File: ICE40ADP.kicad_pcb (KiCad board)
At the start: 2 copper layers, 5 parts, among them J1 Conn_02x20_Odd_Even, J2 Conn_02x20_Odd_Even, J3 Conn_02x20_Odd_Even, J4 Conn_02x20_Odd_Even, J5 Samtec_ASP-134486-01

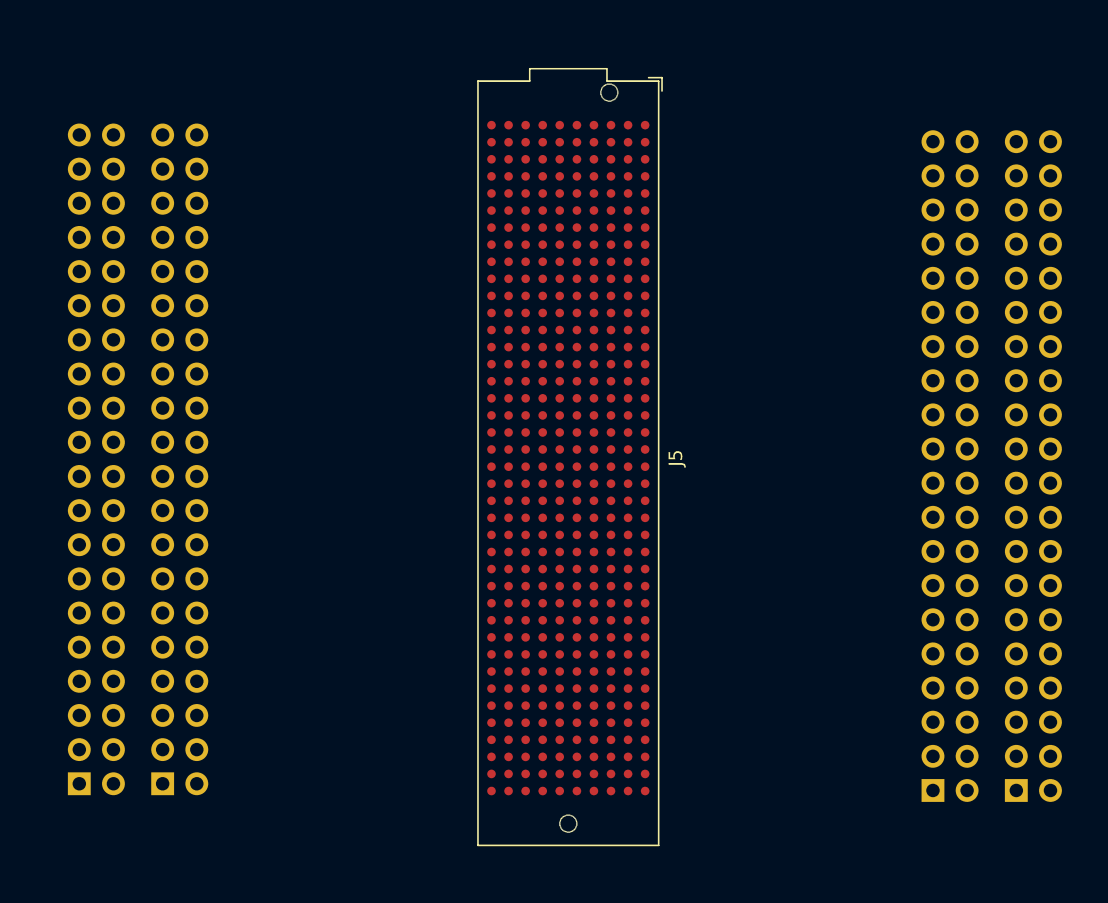
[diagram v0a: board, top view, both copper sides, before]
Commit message: LP lines added. Changed PCB connectors placement
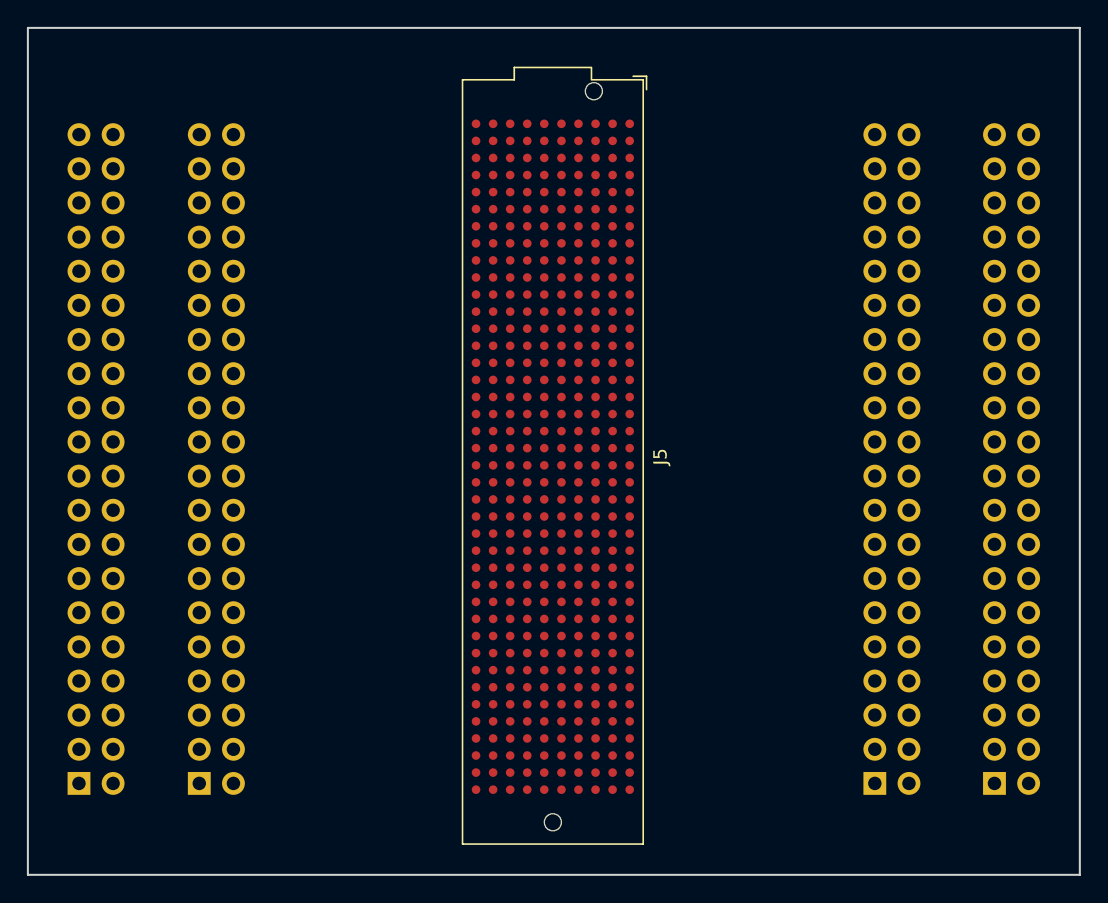
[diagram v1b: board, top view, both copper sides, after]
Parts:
- moved J3 4.36 mm to (170.3, 127.2)
- moved J2 2.73 mm to (120.0, 127.2)
- moved J4 1.71 mm to (179.2, 127.2)
- moved J5 1.15 mm to (146.3, 102.9)
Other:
- board outline added: 78.3 x 63 mm
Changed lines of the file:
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@@
   (general
     (thickness 1.6)
-    (drawings 0)
+    (drawings 4)
     (tracks 0)
     (zones 0)
@@
   )
   (module Connector_PinHeader_2.54mm:PinHeader_2x20_P2.54mm_Vertical (layer B.Cu)
-    (at 111.125001 127.225001)
+    (at 111.1 127.2)
     (descr "Through hole straight pin header, 2x20, 2.54mm pitch, double rows")
     (tags "Through hole pin header THT 2x20 2.54mm double row")
@@
       (effects (font (size 1 1) (thickness 0.15)) (justify mirror))
     )
-    (fp_text value Conn_02x20_Odd_Even (at 1.27 -50.59) (layer B.Fab)
+    (fp_text value Conn_02x20_Odd_Even (at 5.45 -25.35 90) (layer B.Fab)
       (effects (font (size 1 1) (thickness 0.15)) (justify mirror))
     )
@@
   )
   (module Connector_PinHeader_2.54mm:PinHeader_2x20_P2.54mm_Vertical (layer B.Cu)
-    (at 117.325001 127.225001)
+    (at 120.05 127.2)
     (descr "Through hole straight pin header, 2x20, 2.54mm pitch, double rows")
     (tags "Through hole pin header THT 2x20 2.54mm double row")
@@
       (effects (font (size 1 1) (thickness 0.15)) (justify mirror))
     )
-    (fp_text value Conn_02x20_Odd_Even (at 1.27 -50.59) (layer B.Fab)
+    (fp_text value Conn_02x20_Odd_Even (at 5.725 -25.425 90) (layer B.Fab)
       (effects (font (size 1 1) (thickness 0.15)) (justify mirror))
     )
@@
   )
   (module Connector_PinHeader_2.54mm:PinHeader_2x20_P2.54mm_Vertical (layer B.Cu)
-    (at 174.625001 127.725001)
+    (at 170.3 127.2)
     (descr "Through hole straight pin header, 2x20, 2.54mm pitch, double rows")
     (tags "Through hole pin header THT 2x20 2.54mm double row")
@@
       (effects (font (size 1 1) (thickness 0.15)) (justify mirror))
     )
-    (fp_text value Conn_02x20_Odd_Even (at 1.27 -50.59) (layer B.Fab)
+    (fp_text value Conn_02x20_Odd_Even (at -3.275 -25.85 90) (layer B.Fab)
       (effects (font (size 1 1) (thickness 0.15)) (justify mirror))
     )
@@
   )
   (module Connector_PinHeader_2.54mm:PinHeader_2x20_P2.54mm_Vertical (layer B.Cu)
-    (at 180.825001 127.725001)
+    (at 179.2 127.2)
     (descr "Through hole straight pin header, 2x20, 2.54mm pitch, double rows")
     (tags "Through hole pin header THT 2x20 2.54mm double row")
@@
       (effects (font (size 1 1) (thickness 0.15)) (justify mirror))
     )
-    (fp_text value Conn_02x20_Odd_Even (at 1.27 -50.59) (layer B.Fab)
+    (fp_text value Conn_02x20_Odd_Even (at -3 -25.925 90) (layer B.Fab)
       (effects (font (size 1 1) (thickness 0.15)) (justify mirror))
     )
@@
   )
   (module Connector_Samtec:Samtec_FMC_ASP-134486-01_10x40_P1.27mm_Vertical (layer F.Cu)
-    (at 147.5 103 270)
+    (at 146.35 102.9 270)
     (descr http://suddendocs.samtec.com/prints/asp-134486-01-mkt.pdf)
     (tags "FMC HPC")
@@
     )
   )
+  (gr_line (start 107.3 71) (end 185.55 71) (layer Edge.Cuts) (width 0.15))
+  (gr_line (start 107.3 134) (end 185.55 134) (layer Edge.Cuts) (width 0.15))
+  (gr_line (start 107.3 71) (end 107.3 134) (layer Edge.Cuts) (width 0.15))
+  (gr_line (start 185.55 71) (end 185.55 134) (layer Edge.Cuts) (width 0.15))
 )

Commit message: First version of routing
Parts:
- added C1: 4.7uF, Capacitor_SMD:C_0402_1005Metric, B.Cu at (138.6, 123.0)
- added D1: PGB1010603NRHF, Diode_SMD:D_0603_1608Metric, B.Cu at (138.3, 130.4)
- added J6: Micro_SD_Card_Det, Connector_Card:microSD_HC_Hirose_DM3D-SF, B.Cu at (146.4, 127.4)
- added R1: 100K, Resistor_SMD:R_0402_1005Metric, B.Cu at (135.1, 131.2)
- added TP1: TestPoint, TestPoint:TestPoint_Pad_D1.5mm, B.Cu at (146.3, 74.0)
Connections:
- J1 pad 10: (no net) -> CHIPLINK_TX_DAT5
- J1 pad 11: (no net) -> CHIPLINK_TX_DAT4
- J1 pad 12: (no net) -> CHIPLINK_TX_DAT6
- J1 pad 13: (no net) -> CHIPLINK_TX_DAT9
- J1 pad 14: (no net) -> CHIPLINK_TX_DAT10
- J1 pad 15: (no net) -> Earth
- J1 pad 16: (no net) -> Earth
- J1 pad 17: (no net) -> CHIPLINK_TX_DAT7
- J1 pad 18: (no net) -> CHIPLINK_TX_DAT11
- J1 pad 19: (no net) -> CHIPLINK_TX_DAT17
- J1 pad 2: (no net) -> +1V8
- J1 pad 20: (no net) -> CHIPLINK_TX_DAT20
- J1 pad 21: (no net) -> CHIPLINK_TX_DAT8
- J1 pad 22: (no net) -> CHIPLINK_TX_DAT12
- J1 pad 23: (no net) -> Earth
- J1 pad 24: (no net) -> Earth
- J1 pad 25: (no net) -> CHIPLINK_TX_CLK
- J1 pad 26: (no net) -> CHIPLINK_TX_DAT14
- J1 pad 27: (no net) -> CHIPLINK_TX_DAT13
- J1 pad 28: (no net) -> CHIPLINK_TX_DAT16
- J1 pad 29: (no net) -> CHIPLINK_TX_DAT15
- J1 pad 30: (no net) -> CHIPLINK_TX_DAT22
- J1 pad 31: (no net) -> Earth
- J1 pad 32: (no net) -> Earth
- J1 pad 33: (no net) -> CHIPLINK_TX_DAT18
- J1 pad 34: (no net) -> CHIPLINK_TX_DAT21
- J1 pad 35: (no net) -> CHIPLINK_TX_DAT19
- J1 pad 36: (no net) -> CHIPLINK_TX_DAT25
- J1 pad 37: (no net) -> CHIPLINK_TX_DAT23
- J1 pad 38: (no net) -> CHIPLINK_TX_DAT24
- J1 pad 39: (no net) -> Earth
- J1 pad 4: (no net) -> CHIPLINK_TX_DAT0
- J1 pad 40: (no net) -> Earth
- J1 pad 5: (no net) -> CHIPLINK_TX_DAT2
- J1 pad 6: (no net) -> CHIPLINK_TX_DAT1
- J1 pad 7: (no net) -> Earth
- J1 pad 8: (no net) -> Earth
- J1 pad 9: (no net) -> CHIPLINK_TX_DAT3
- J2 pad 1: (no net) -> /Sheet5CA0FCBB/SDIO_DAT2
- J2 pad 15: (no net) -> Earth
- J2 pad 16: (no net) -> Earth
- J2 pad 2: (no net) -> /Sheet5CA0FCBB/+3V3
- J2 pad 23: (no net) -> Earth
- J2 pad 24: (no net) -> Earth
- J2 pad 3: (no net) -> /Sheet5CA0FCBB/SDIO_DAT3
- J2 pad 31: (no net) -> Earth
- J2 pad 32: (no net) -> Earth
- J2 pad 39: (no net) -> Earth
- J2 pad 4: (no net) -> /Sheet5CA0FCBB/SDIO_DAT0
- J2 pad 40: (no net) -> Earth
- J2 pad 5: (no net) -> /Sheet5CA0FCBB/SDIO_CMD
- J2 pad 6: (no net) -> /Sheet5CA0FCBB/SDIO_DAT1
- J2 pad 7: (no net) -> Earth
- J2 pad 8: (no net) -> Earth
- J2 pad 9: (no net) -> /Sheet5CA0FCBB/SDIO_CLK
- J3 pad 1: (no net) -> CHIPLINK_RX_DAT26
- J3 pad 11: (no net) -> CHIPLINK_RX_DAT18
- J3 pad 12: (no net) -> CHIPLINK_RX_DAT22
- J3 pad 13: (no net) -> CHIPLINK_RX_DAT19
- J3 pad 14: (no net) -> CHIPLINK_RX_DAT16
- J3 pad 15: (no net) -> Earth
- J3 pad 16: (no net) -> Earth
- J3 pad 17: (no net) -> CHIPLINK_RX_DAT17
- J3 pad 18: (no net) -> CHIPLINK_RX_DAT15
- J3 pad 19: (no net) -> CHIPLINK_RX_DAT9
- J3 pad 2: (no net) -> +1V8
- J3 pad 20: (no net) -> CHIPLINK_RX_DAT14
- J3 pad 21: (no net) -> CHIPLINK_RX_DAT13
- J3 pad 22: (no net) -> CHIPLINK_RX_CLK
- J3 pad 23: (no net) -> Earth
- J3 pad 24: (no net) -> Earth
- J3 pad 25: (no net) -> CHIPLINK_RX_DAT11
- J3 pad 26: (no net) -> CHIPLINK_RX_DAT12
- J3 pad 27: (no net) -> CHIPLINK_RX_DAT10
- J3 pad 28: (no net) -> CHIPLINK_RX_DAT8
- J3 pad 29: (no net) -> CHIPLINK_RX_DAT7
- J3 pad 3: (no net) -> CHIPLINK_RX_DAT20
- J3 pad 30: (no net) -> CHIPLINK_RX_DAT4
- J3 pad 31: (no net) -> Earth
- J3 pad 32: (no net) -> Earth
- J3 pad 33: (no net) -> CHIPLINK_RX_DAT3
- J3 pad 34: (no net) -> CHIPLINK_RX_DAT6
- J3 pad 35: (no net) -> CHIPLINK_RX_DAT1
- J3 pad 36: (no net) -> CHIPLINK_RX_DAT5
- J3 pad 37: (no net) -> CHIPLINK_RX_DAT0
- J3 pad 38: (no net) -> CHIPLINK_RX_DAT2
- J3 pad 39: (no net) -> Earth
- J3 pad 4: (no net) -> CHIPLINK_RX_DAT25
- J3 pad 40: (no net) -> Earth
- J3 pad 5: (no net) -> CHIPLINK_RX_DAT23
- J3 pad 6: (no net) -> CHIPLINK_RX_DAT21
- J3 pad 7: (no net) -> Earth
- J3 pad 8: (no net) -> Earth
- J3 pad 9: (no net) -> CHIPLINK_RX_DAT24
- J4 pad 15: (no net) -> Earth
- J4 pad 16: (no net) -> Earth
- J4 pad 18: (no net) -> CHIPLINK_RX_DAT27
- J4 pad 2: (no net) -> +1V8
- J4 pad 20: (no net) -> CHIPLINK_TX_RST
- J4 pad 21: (no net) -> CHIPLINK_RX_SEND
- J4 pad 23: (no net) -> Earth
- J4 pad 24: (no net) -> Earth
- J4 pad 25: (no net) -> CHIPLINK_RX_DAT31
- J4 pad 26: (no net) -> CHIPLINK_RX_RST
- J4 pad 27: (no net) -> CHIPLINK_RX_DAT29
- J4 pad 28: (no net) -> CHIPLINK_TX_SEND
- J4 pad 29: (no net) -> CHIPLINK_RX_DAT28
- J4 pad 30: (no net) -> CHIPLINK_RX_DAT30
- J4 pad 31: (no net) -> Earth
- J4 pad 32: (no net) -> Earth
- J4 pad 33: (no net) -> CHIPLINK_TX_DAT31
- J4 pad 34: (no net) -> CHIPLINK_TX_DAT30
- J4 pad 35: (no net) -> CHIPLINK_TX_DAT28
- J4 pad 36: (no net) -> CHIPLINK_TX_DAT29
- J4 pad 37: (no net) -> CHIPLINK_TX_DAT27
- J4 pad 38: (no net) -> CHIPLINK_TX_DAT26
- J4 pad 39: (no net) -> Earth
- J4 pad 4: (no net) -> RESET_N
- J4 pad 40: (no net) -> Earth
- J4 pad 6: (no net) -> /Sheet5CA0FCBB/SDIO_CD
- J4 pad 7: (no net) -> Earth
- J4 pad 8: (no net) -> Earth
- J5 pad A1: (no net) -> Earth
- J5 pad A12: (no net) -> Earth
- J5 pad A13: (no net) -> Earth
- J5 pad A16: (no net) -> Earth
- J5 pad A17: (no net) -> Earth
- J5 pad A20: (no net) -> Earth
- J5 pad A21: (no net) -> Earth
- J5 pad A24: (no net) -> Earth
- J5 pad A25: (no net) -> Earth
- J5 pad A28: (no net) -> Earth
- J5 pad A29: (no net) -> Earth
- J5 pad A32: (no net) -> Earth
- J5 pad A33: (no net) -> Earth
- J5 pad A36: (no net) -> Earth
- J5 pad A37: (no net) -> Earth
- J5 pad A4: (no net) -> Earth
- J5 pad A40: (no net) -> Earth
- J5 pad A5: (no net) -> Earth
- J5 pad A8: (no net) -> Earth
- J5 pad A9: (no net) -> Earth
- J5 pad B10: (no net) -> Earth
- J5 pad B11: (no net) -> Earth
- J5 pad B14: (no net) -> Earth
- J5 pad B15: (no net) -> Earth
- J5 pad B18: (no net) -> Earth
- J5 pad B19: (no net) -> Earth
- J5 pad B2: (no net) -> Earth
- J5 pad B22: (no net) -> Earth
- J5 pad B23: (no net) -> Earth
- J5 pad B26: (no net) -> Earth
- J5 pad B27: (no net) -> Earth
- J5 pad B3: (no net) -> Earth
- J5 pad B30: (no net) -> Earth
- J5 pad B31: (no net) -> Earth
- J5 pad B34: (no net) -> Earth
- J5 pad B35: (no net) -> Earth
- J5 pad B38: (no net) -> Earth
- J5 pad B39: (no net) -> Earth
- J5 pad B6: (no net) -> Earth
- J5 pad B7: (no net) -> Earth
- J5 pad C1: (no net) -> Earth
- J5 pad C10: (no net) -> CHIPLINK_TX_DAT12
- J5 pad C11: (no net) -> CHIPLINK_TX_DAT13
- J5 pad C12: (no net) -> Earth
- J5 pad C13: (no net) -> Earth
- J5 pad C14: (no net) -> CHIPLINK_TX_DAT20
- J5 pad C15: (no net) -> CHIPLINK_TX_DAT21
- J5 pad C16: (no net) -> Earth
- J5 pad C17: (no net) -> Earth
- J5 pad C18: (no net) -> CHIPLINK_TX_DAT28
- J5 pad C19: (no net) -> CHIPLINK_TX_DAT29
- J5 pad C20: (no net) -> Earth
- J5 pad C21: (no net) -> Earth
- J5 pad C22: (no net) -> CHIPLINK_RX_DAT2
- J5 pad C23: (no net) -> CHIPLINK_RX_DAT3
- J5 pad C24: (no net) -> Earth
- J5 pad C25: (no net) -> Earth
- J5 pad C26: (no net) -> CHIPLINK_RX_DAT20
- J5 pad C27: (no net) -> CHIPLINK_RX_DAT21
- J5 pad C28: (no net) -> Earth
- J5 pad C29: (no net) -> Earth
- J5 pad C32: (no net) -> Earth
- J5 pad C33: (no net) -> Earth
- J5 pad C35: (no net) -> /Sheet5CA0FCF5/12P0V_FMC
- J5 pad C36: (no net) -> Earth
- J5 pad C37: (no net) -> /Sheet5CA0FCF5/12P0V_FMC
- J5 pad C38: (no net) -> Earth
- J5 pad C4: (no net) -> Earth
- J5 pad C40: (no net) -> Earth
- J5 pad C5: (no net) -> Earth
- J5 pad C8: (no net) -> Earth
- J5 pad C9: (no net) -> Earth
- J5 pad D10: (no net) -> Earth
- J5 pad D11: (no net) -> CHIPLINK_TX_DAT10
- J5 pad D12: (no net) -> CHIPLINK_TX_DAT11
- J5 pad D13: (no net) -> Earth
- J5 pad D14: (no net) -> CHIPLINK_TX_DAT18
- J5 pad D15: (no net) -> CHIPLINK_TX_DAT19
- J5 pad D16: (no net) -> Earth
- J5 pad D17: (no net) -> CHIPLINK_TX_DAT26
- J5 pad D18: (no net) -> CHIPLINK_TX_DAT27
- J5 pad D19: (no net) -> Earth
- J5 pad D2: (no net) -> Earth
- J5 pad D20: (no net) -> CHIPLINK_RX_DAT0
- J5 pad D21: (no net) -> CHIPLINK_RX_DAT1
- J5 pad D22: (no net) -> Earth
- J5 pad D23: (no net) -> CHIPLINK_RX_DAT12
- J5 pad D24: (no net) -> CHIPLINK_RX_DAT13
- J5 pad D25: (no net) -> Earth
- J5 pad D26: (no net) -> CHIPLINK_RX_DAT18
- J5 pad D27: (no net) -> CHIPLINK_RX_DAT19
- J5 pad D28: (no net) -> Earth
- J5 pad D3: (no net) -> Earth
- J5 pad D37: (no net) -> Earth
- J5 pad D39: (no net) -> Earth
- J5 pad D6: (no net) -> Earth
- J5 pad D7: (no net) -> Earth
- J5 pad D8: (no net) -> CHIPLINK_TX_DAT2
- J5 pad D9: (no net) -> CHIPLINK_TX_DAT3
- J5 pad E1: (no net) -> Earth
- J5 pad E11: (no net) -> Earth
- J5 pad E14: (no net) -> Earth
- J5 pad E17: (no net) -> Earth
- J5 pad E20: (no net) -> Earth
- J5 pad E23: (no net) -> Earth
- J5 pad E26: (no net) -> Earth
- J5 pad E29: (no net) -> Earth
- J5 pad E32: (no net) -> Earth
- J5 pad E35: (no net) -> Earth
- J5 pad E38: (no net) -> Earth
- J5 pad E4: (no net) -> Earth
- J5 pad E40: (no net) -> Earth
- J5 pad E5: (no net) -> Earth
- J5 pad E8: (no net) -> Earth
- J5 pad F12: (no net) -> Earth
- J5 pad F15: (no net) -> Earth
- J5 pad F18: (no net) -> Earth
- J5 pad F2: (no net) -> Earth
- J5 pad F21: (no net) -> Earth
- J5 pad F24: (no net) -> Earth
- J5 pad F27: (no net) -> Earth
- J5 pad F3: (no net) -> Earth
- J5 pad F30: (no net) -> Earth
- J5 pad F33: (no net) -> Earth
- J5 pad F36: (no net) -> Earth
- J5 pad F39: (no net) -> Earth
- J5 pad F6: (no net) -> Earth
- J5 pad F9: (no net) -> Earth
- J5 pad G1: (no net) -> Earth
- J5 pad G10: (no net) -> CHIPLINK_TX_DAT7
- J5 pad G11: (no net) -> Earth
- J5 pad G12: (no net) -> CHIPLINK_TX_DAT16
- J5 pad G13: (no net) -> CHIPLINK_TX_DAT17
- J5 pad G14: (no net) -> Earth
- J5 pad G15: (no net) -> CHIPLINK_TX_DAT24
- J5 pad G16: (no net) -> CHIPLINK_TX_DAT25
- J5 pad G17: (no net) -> Earth
- J5 pad G18: (no net) -> CHIPLINK_TX_SEND
- J5 pad G19: (no net) -> CHIPLINK_TX_RST
- J5 pad G2: (no net) -> CHIPLINK_RX_CLK
- J5 pad G20: (no net) -> Earth
- J5 pad G21: (no net) -> CHIPLINK_RX_DAT6
- J5 pad G22: (no net) -> CHIPLINK_RX_DAT7
- J5 pad G23: (no net) -> Earth
- J5 pad G24: (no net) -> CHIPLINK_RX_DAT10
- J5 pad G25: (no net) -> CHIPLINK_RX_DAT11
- J5 pad G26: (no net) -> Earth
- J5 pad G27: (no net) -> CHIPLINK_RX_DAT16
- J5 pad G28: (no net) -> CHIPLINK_RX_DAT17
- J5 pad G29: (no net) -> Earth
- J5 pad G30: (no net) -> CHIPLINK_RX_DAT24
- J5 pad G31: (no net) -> CHIPLINK_RX_DAT25
- J5 pad G32: (no net) -> Earth
- J5 pad G33: (no net) -> CHIPLINK_RX_DAT28
- J5 pad G34: (no net) -> CHIPLINK_RX_DAT29
- J5 pad G35: (no net) -> Earth
- J5 pad G36: (no net) -> CHIPLINK_RX_SEND
- J5 pad G37: (no net) -> CHIPLINK_RX_RST
- J5 pad G38: (no net) -> Earth
- J5 pad G4: (no net) -> Earth
- J5 pad G40: (no net) -> Earth
- J5 pad G5: (no net) -> Earth
- J5 pad G6: (no net) -> CHIPLINK_TX_DAT0
- J5 pad G7: (no net) -> CHIPLINK_TX_DAT1
- J5 pad G8: (no net) -> Earth
- J5 pad G9: (no net) -> CHIPLINK_TX_DAT6
- J5 pad H1: (no net) -> +1V8
- J5 pad H10: (no net) -> CHIPLINK_TX_DAT8
- J5 pad H11: (no net) -> CHIPLINK_TX_DAT9
- J5 pad H12: (no net) -> Earth
- J5 pad H13: (no net) -> CHIPLINK_TX_DAT14
- J5 pad H14: (no net) -> CHIPLINK_TX_DAT15
- J5 pad H15: (no net) -> Earth
- J5 pad H16: (no net) -> CHIPLINK_TX_DAT22
- J5 pad H17: (no net) -> CHIPLINK_TX_DAT23
- J5 pad H18: (no net) -> Earth
- J5 pad H19: (no net) -> CHIPLINK_TX_DAT30
- J5 pad H2: (no net) -> Earth
- J5 pad H20: (no net) -> CHIPLINK_TX_DAT31
- J5 pad H21: (no net) -> Earth
- J5 pad H22: (no net) -> CHIPLINK_RX_DAT4
- J5 pad H23: (no net) -> CHIPLINK_RX_DAT5
- J5 pad H24: (no net) -> Earth
- J5 pad H25: (no net) -> CHIPLINK_RX_DAT8
- J5 pad H26: (no net) -> CHIPLINK_RX_DAT9
- J5 pad H27: (no net) -> Earth
- J5 pad H28: (no net) -> CHIPLINK_RX_DAT14
- J5 pad H29: (no net) -> CHIPLINK_RX_DAT15
- J5 pad H3: (no net) -> Earth
- J5 pad H30: (no net) -> Earth
- J5 pad H31: (no net) -> CHIPLINK_RX_DAT22
- J5 pad H32: (no net) -> CHIPLINK_RX_DAT23
- J5 pad H33: (no net) -> Earth
- J5 pad H34: (no net) -> CHIPLINK_RX_DAT26
- J5 pad H35: (no net) -> CHIPLINK_RX_DAT27
- J5 pad H36: (no net) -> Earth
- J5 pad H37: (no net) -> CHIPLINK_RX_DAT30
- J5 pad H38: (no net) -> CHIPLINK_RX_DAT31
- J5 pad H39: (no net) -> Earth
- J5 pad H4: (no net) -> CHIPLINK_TX_CLK
- J5 pad H5: (no net) -> RESET_N
- J5 pad H6: (no net) -> Earth
- J5 pad H7: (no net) -> CHIPLINK_TX_DAT4
- J5 pad H8: (no net) -> CHIPLINK_TX_DAT5
- J5 pad H9: (no net) -> Earth
- J5 pad J1: (no net) -> Earth
- J5 pad J11: (no net) -> Earth
- J5 pad J14: (no net) -> Earth
- J5 pad J17: (no net) -> Earth
- J5 pad J20: (no net) -> Earth
- J5 pad J23: (no net) -> Earth
- J5 pad J26: (no net) -> Earth
- J5 pad J29: (no net) -> Earth
- J5 pad J32: (no net) -> Earth
- J5 pad J35: (no net) -> Earth
- J5 pad J38: (no net) -> Earth
- J5 pad J4: (no net) -> Earth
- J5 pad J40: (no net) -> Earth
- J5 pad J5: (no net) -> Earth
- J5 pad J8: (no net) -> Earth
- J5 pad K12: (no net) -> Earth
- J5 pad K15: (no net) -> Earth
- J5 pad K18: (no net) -> Earth
- J5 pad K2: (no net) -> Earth
- J5 pad K21: (no net) -> Earth
- J5 pad K24: (no net) -> Earth
- J5 pad K27: (no net) -> Earth
- J5 pad K3: (no net) -> Earth
- J5 pad K30: (no net) -> Earth
- J5 pad K33: (no net) -> Earth
- J5 pad K36: (no net) -> Earth
- J5 pad K39: (no net) -> Earth
- J5 pad K6: (no net) -> Earth
- J5 pad K9: (no net) -> Earth
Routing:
- net Earth: track 0.00 -> 203.1 mm, vias 0 -> 133
- net +1V8: track 0.00 -> 197.9 mm, vias 0 -> 2
- net CHIPLINK_RX_SEND: track 0.00 -> 94.3 mm
- net RESET_N: track 0.00 -> 92.7 mm, vias 0 -> 1
- net CHIPLINK_TX_DAT0: track 0.00 -> 88.9 mm
- net CHIPLINK_RX_DAT30: track 0.00 -> 87.4 mm, vias 0 -> 1
- net CHIPLINK_RX_DAT27: track 0.00 -> 77.0 mm
- net CHIPLINK_TX_DAT2: track 0.00 -> 70.7 mm, vias 0 -> 2
- net CHIPLINK_RX_RST: track 0.00 -> 66.1 mm, vias 0 -> 1
- net CHIPLINK_TX_DAT1: track 0.00 -> 62.0 mm, vias 0 -> 2
- net CHIPLINK_TX_DAT9: track 0.00 -> 61.3 mm, vias 0 -> 2
- net CHIPLINK_RX_DAT31: track 0.00 -> 61.3 mm, vias 0 -> 1
- net CHIPLINK_TX_DAT30: track 0.00 -> 61.3 mm, vias 0 -> 1
- net CHIPLINK_RX_DAT28: track 0.00 -> 60.6 mm, vias 0 -> 1
- net CHIPLINK_TX_DAT24: track 0.00 -> 59.5 mm
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- added copper zone on B.Cu, net +1V8
- added copper zone on In1.Cu, net Earth
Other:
- copper layers 2 -> 4
- net class BigPower added: clearance 0.2, trace_width 0.45, via_dia 0.45, via_drill 0.2
- net class Main added: clearance 0.1, trace_width 0.1, via_dia 0.45, via_drill 0.2
- net class Power added: clearance 0.2, trace_width 0.2, via_dia 0.45, via_drill 0.2
- rule trace_min: 0.2 -> 0.1
- rule via_min_drill: 0.3 -> 0.2
- rule via_min_size: 0.4 -> 0.45

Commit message: Production version #1
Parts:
- added G***: LOGO, ICE40ADP:forksand, F.Cu at (130.7, 103.8)
- added G***: LOGO, ICE40ADP:logo, F.Cu at (161.3, 103.1)
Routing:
- net CHIPLINK_RX_DAT13: track 24.3 -> 100.0 mm
- net CHIPLINK_RX_DAT19: track 25.0 -> 100.0 mm
- net CHIPLINK_RX_DAT18: track 27.0 -> 100.0 mm
- net CHIPLINK_RX_DAT24: track 28.5 -> 100.0 mm
- net CHIPLINK_TX_DAT25: track 37.4 -> 107.8 mm
- net CHIPLINK_RX_DAT20: track 30.0 -> 100.0 mm
- net CHIPLINK_RX_DAT9: track 30.5 -> 100.0 mm
- net CHIPLINK_RX_DAT16: track 31.1 -> 100.0 mm
- net CHIPLINK_RX_DAT12: track 31.1 -> 100.0 mm
- net CHIPLINK_TX_DAT14: track 32.2 -> 100.1 mm
- net CHIPLINK_TX_DAT16: track 32.6 -> 100.1 mm
- net CHIPLINK_TX_DAT22: track 32.7 -> 100.0 mm
- net CHIPLINK_RX_DAT22: track 33.5 -> 100.0 mm
- net CHIPLINK_RX_DAT10: track 33.6 -> 100.0 mm
- net CHIPLINK_RX_DAT25: track 33.9 -> 100.0 mm
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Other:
- board text added: "Copyright (C) 2019 Fork Sand, Inc. GPLv3+"
